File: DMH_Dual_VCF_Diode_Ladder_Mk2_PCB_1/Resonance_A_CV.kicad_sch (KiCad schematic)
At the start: 25 parts, among them J21 Conn_01x06_PinHeader, Q1 BC548, Q2 BC548, U1 TL074

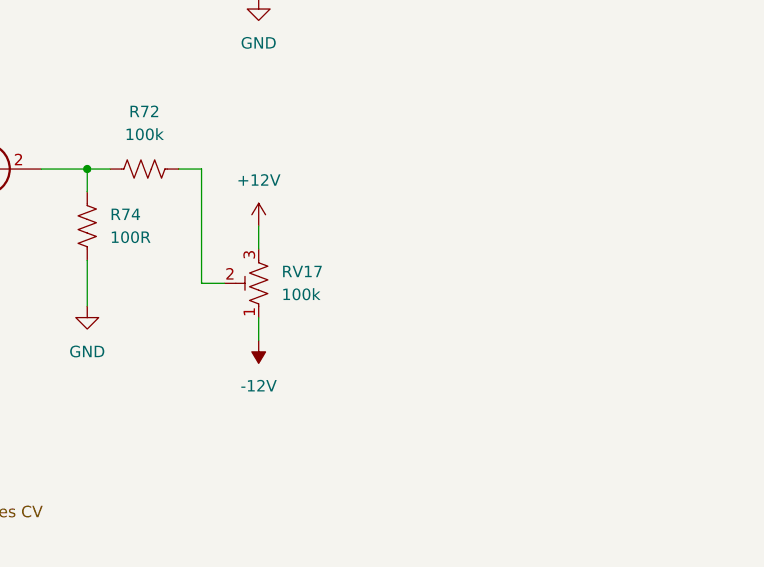
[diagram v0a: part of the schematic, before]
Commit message: Added trim pot functions to silkscreen
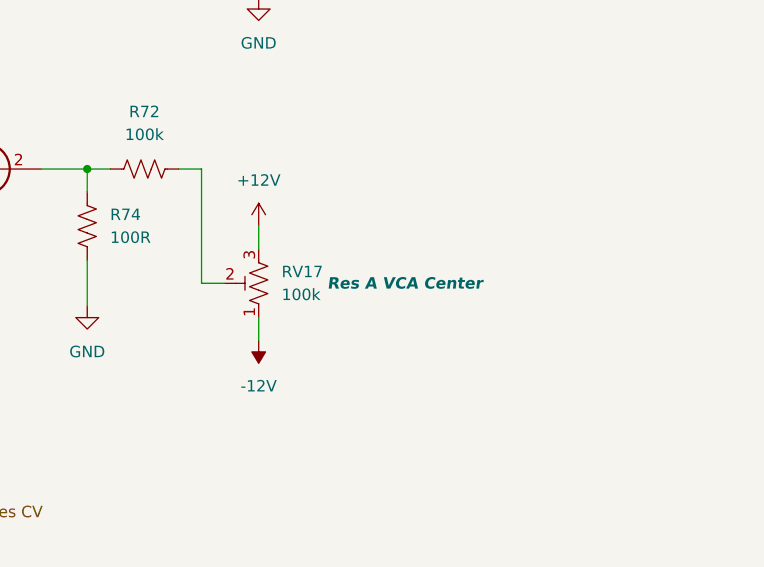
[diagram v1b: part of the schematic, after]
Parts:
- RV17: Function (none) -> Res A VCA Center
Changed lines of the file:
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@@
 		(on_board yes)
 		(dnp no)
-		(fields_autoplaced yes)
 		(property "Reference" "RV17"
 			(at 224.79 100.3299 0)
@@
 			)
 		)
+		(property "Function" "Res A VCA Center"
+			(at 238.506 101.6 0)
+			(effects
+				(font
+					(size 1.27 1.27)
+					(thickness 0.254)
+					(bold yes)
+					(italic yes)
+				)
+			)
+		)

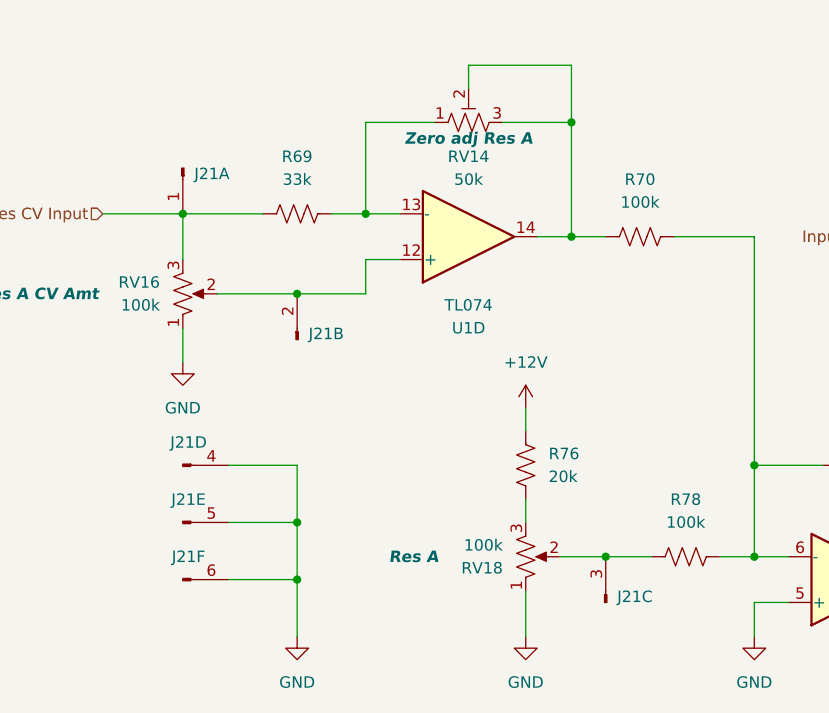
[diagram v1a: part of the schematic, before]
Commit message: Adjusted pin header connections
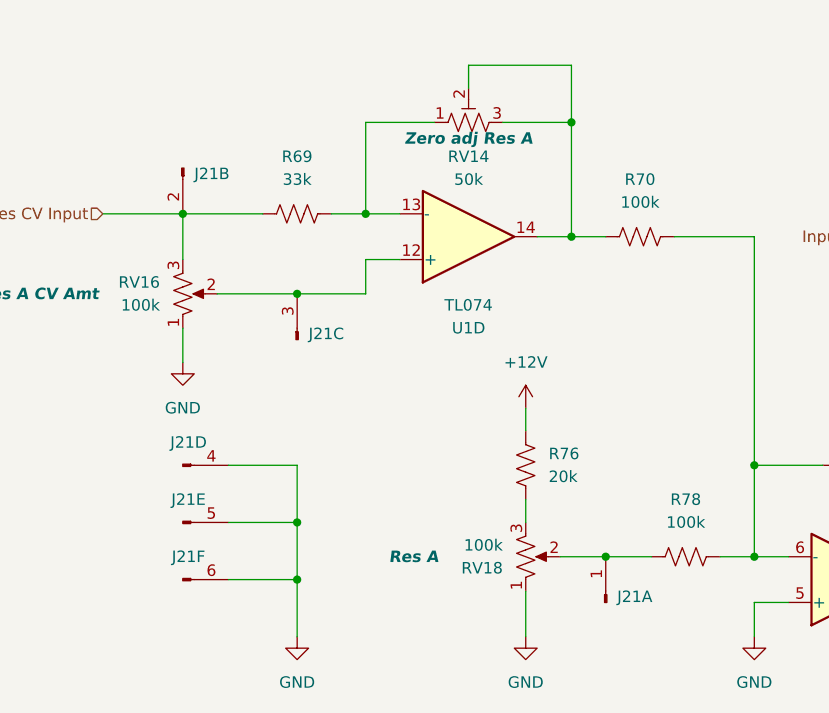
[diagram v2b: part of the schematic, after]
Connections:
- net Res CV Input: now also J21.2 (Pin_2); no longer J21.1 (Pin_1)
- net at RV16.2, U1.12 (+): now also J21.3 (Pin_3); no longer J21.2 (Pin_2)
- net at R78.1, RV18.2: now also J21.1 (Pin_1); no longer J21.3 (Pin_3)
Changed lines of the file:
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@@
 		(lib_id "SynthStuff:Conn_01x06_PinHeader")
 		(at 76.2 100.33 90)
-		(unit 2)
+		(unit 3)
 		(exclude_from_sim no)
 		(in_bom yes)
@@
 				(path "/58f4306d-5387-4983-bb08-41a2313fd315/ad5c5475-8483-41b0-97cc-617422d54799"
 					(reference "J21")
-					(unit 2)
+					(unit 3)
 				)
 			)
@@
 		(lib_id "SynthStuff:Conn_01x06_PinHeader")
 		(at 63.5 81.28 270)
-		(unit 1)
+		(unit 2)
 		(exclude_from_sim no)
 		(in_bom yes)
@@
 				(path "/58f4306d-5387-4983-bb08-41a2313fd315/ad5c5475-8483-41b0-97cc-617422d54799"
 					(reference "J21")
-					(unit 1)
+					(unit 2)
 				)
 			)
@@
 		(lib_id "SynthStuff:Conn_01x06_PinHeader")
 		(at 110.49 129.54 90)
-		(unit 3)
+		(unit 1)
 		(exclude_from_sim no)
 		(in_bom yes)
@@
 				(path "/58f4306d-5387-4983-bb08-41a2313fd315/ad5c5475-8483-41b0-97cc-617422d54799"
 					(reference "J21")
-					(unit 3)
-				)
-			)
+					(unit 1)
+				)
+			)

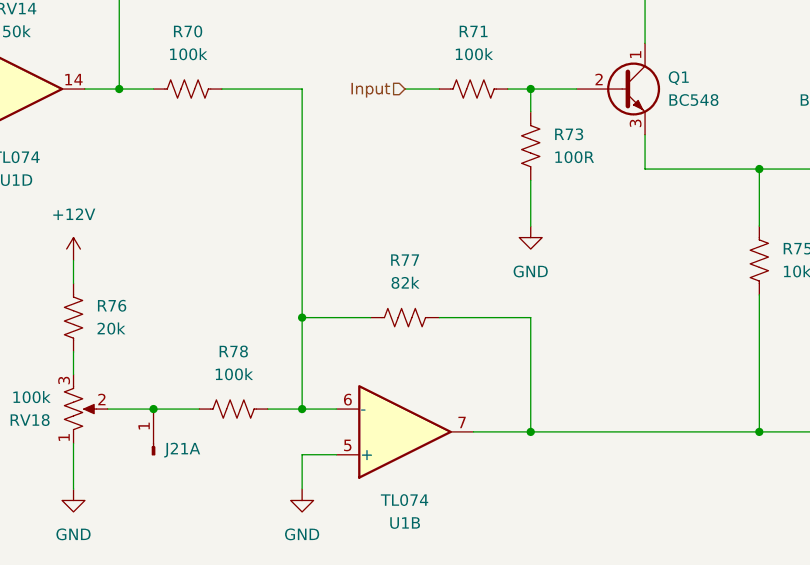
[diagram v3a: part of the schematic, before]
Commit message: Changed VCA CV summing stage feedback to 100k
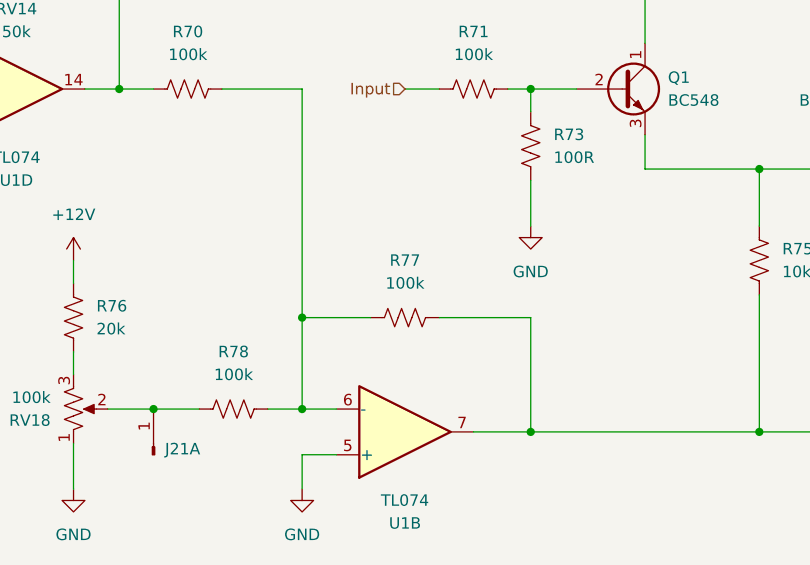
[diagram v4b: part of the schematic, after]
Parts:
- R77: value 82k -> 100k
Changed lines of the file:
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@@
 			)
 		)
-		(property "Value" "82k"
+		(property "Value" "100k"
 			(at 138.43 110.49 90)
 			(effects

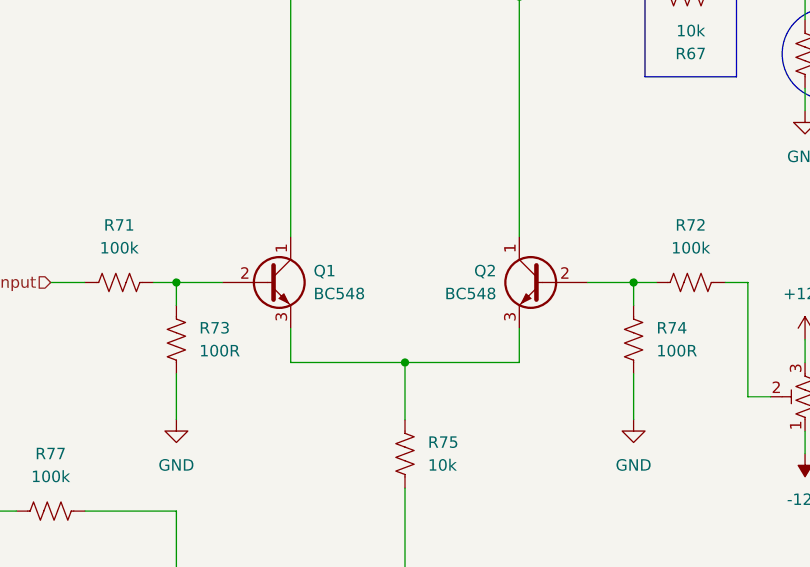
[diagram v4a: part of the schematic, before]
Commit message: Adding buffered input to CV3 - in progress
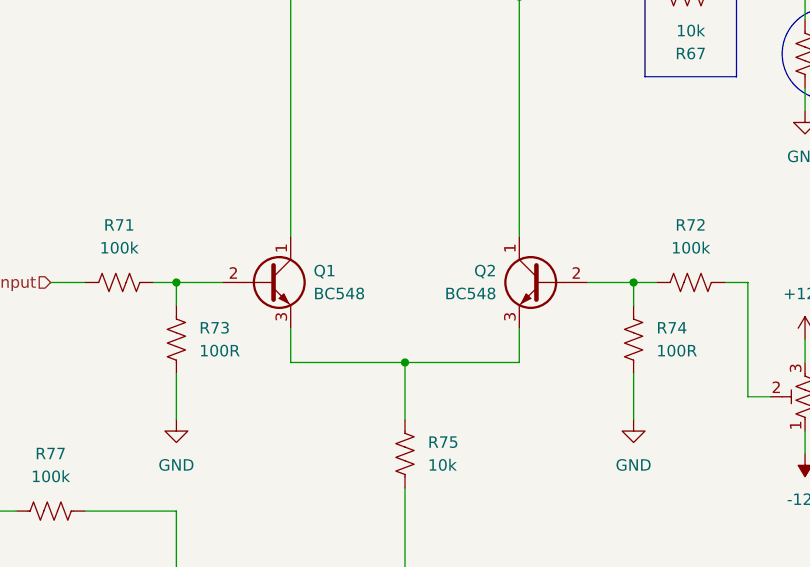
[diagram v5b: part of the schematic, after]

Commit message: validation ongoing
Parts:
- R64, R68: value 100k -> 2k2
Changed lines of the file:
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@@
 			)
 		)
-		(property "Value" "100k"
+		(property "Value" "2k2"
 			(at 224.79 64.7699 0)
 			(effects
@@
 			)
 		)
-		(property "Value" "100k"
+		(property "Value" "2k2"
 			(at 234.95 34.29 90)
 			(effects

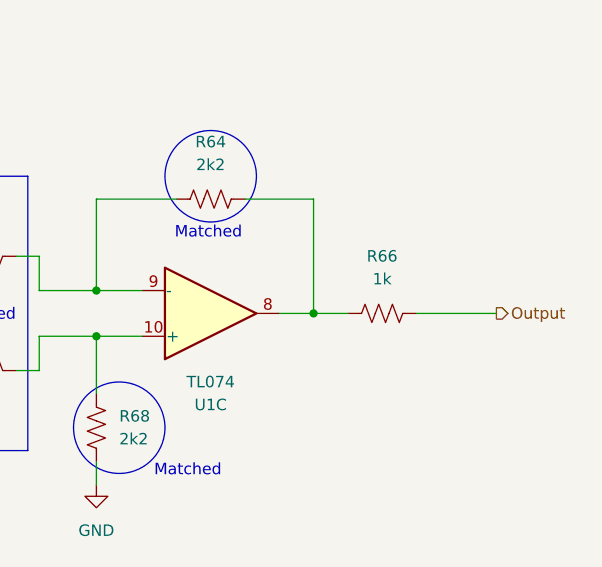
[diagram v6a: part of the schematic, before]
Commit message: Updated various resistor values
... and deleted all VCAs output 1k resistors
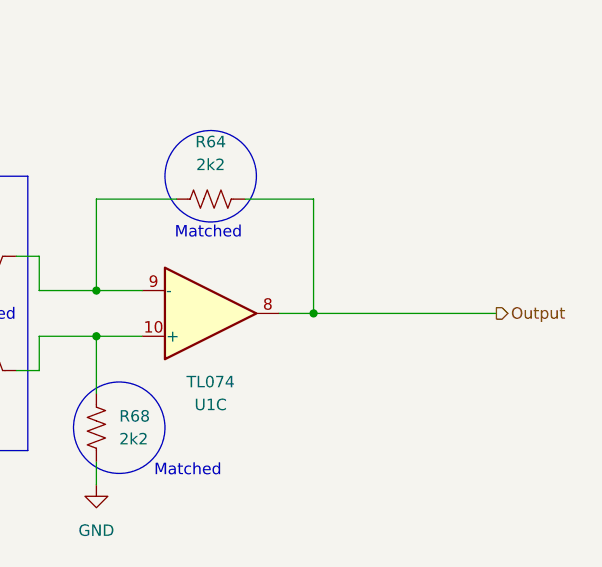
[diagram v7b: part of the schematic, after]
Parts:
- removed R66: 1k, Resistor_THT:R_Axial_DIN0207_L6.3mm_D2.5mm_P7.62mm_Horizontal, symbol Device:R_US
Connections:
- net Output: now also R64.1, U1.8
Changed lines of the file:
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@@
-	(wire
-		(pts
-			(xy 257.81 50.8) (xy 266.7 50.8)
-		)
-		(stroke
-			(width 0)
-			(type default)
-		)
-	)
 	(wire
 		(pts
@@
 	(wire
 		(pts
-			(xy 246.38 50.8) (xy 250.19 50.8)
+			(xy 246.38 50.8) (xy 266.7 50.8)
 		)
 		(stroke
@@
 					(unit 1)
 				)
-			)
-		)
-	)
-	(symbol
-		(lib_id "Device:R_US")
-		(at 254 50.8 270)
-		(unit 1)
-		(exclude_from_sim no)
-		(in_bom yes)
-		(on_board yes)
-		(dnp no)
-		(fields_autoplaced yes)
-		(property "Reference" "R66"
-			(at 254 44.45 90)
-			(effects
-				(font
-					(size 1.27 1.27)
-				)
-			)
-		)
-		(property "Value" "1k"
-			(at 254 46.99 90)
-			(effects
-				(font
-					(size 1.27 1.27)
-				)
-			)
-		)
-		(property "Footprint" "Resistor_THT:R_Axial_DIN0207_L6.3mm_D2.5mm_P7.62mm_Horizontal"
-			(at 253.746 51.816 90)
-			(effects
-				(font
-					(size 1.27 1.27)
-				)
-				(hide yes)
-			)
-		)
-		(property "Datasheet" "~"
-			(at 254 50.8 0)
-			(effects
-				(font
-					(size 1.27 1.27)
-				)
-				(hide yes)
-			)
-		)
-		(property "Description" "Resistor, US symbol"
-			(at 254 50.8 0)
-			(effects
-				(font
-					(size 1.27 1.27)
-				)
-				(hide yes)
-			)
-		)
-		(property "Function" ""
-			(at 254 50.8 0)
-			(effects
-				(font
-					(size 1.27 1.27)
-				)
-			)
-		)
-		(pin "1"
-		)
-		(pin "2"
-		)
-		(instances
-			(project "DMH_Dual_VCF_Diode_Ladder_Mk2_PCB_1"
-				(path "/58f4306d-5387-4983-bb08-41a2313fd315/ad5c5475-8483-41b0-97cc-617422d54799"
-					(reference "R66")
-					(unit 1)
-				)

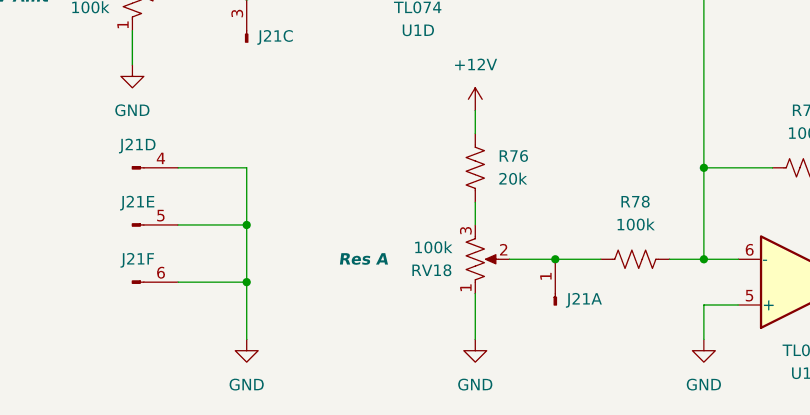
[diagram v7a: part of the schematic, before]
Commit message: Changed Resonance pots to Taper C type
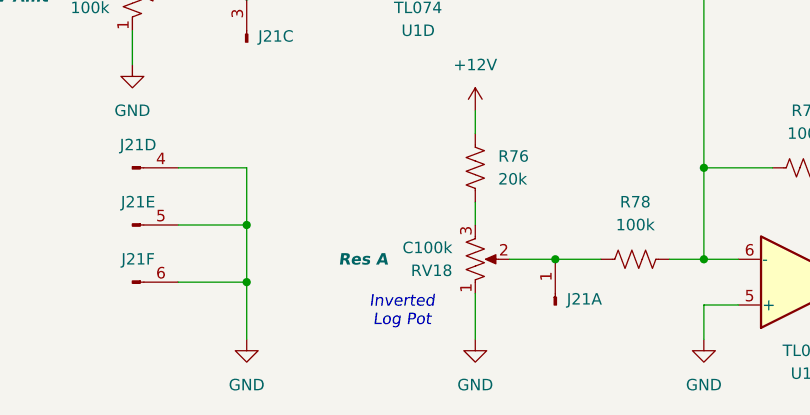
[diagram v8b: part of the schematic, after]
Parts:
- RV18: value 100k -> C100k
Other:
- note added: "Inverted Log Pot"
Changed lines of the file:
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@@
+		)
+	)
+	(text "Inverted\nLog Pot"
+		(exclude_from_sim no)
+		(at 93.472 130.302 0)
+		(effects
+			(font
+				(size 1.27 1.27)
+				(italic yes)
+			)
 		)
 	)
@@
 			)
 		)
-		(property "Value" "100k"
+		(property "Value" "C100k"
 			(at 99.06 123.1901 0)
 			(effects
